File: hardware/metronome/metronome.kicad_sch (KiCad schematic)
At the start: 57 parts, among them J1 USB_C_Receptacle_USB2.0, J2 Conn_01x03_Pin, J3 Conn_01x04_Pin, J4 AudioJack3_Ground, SW1 RotaryEncoder_Switch, SW2 SW_SPST, SW3 SW_SPST, SW4 SW_SPST, SW5 SW_SPST, U1 ATtiny412, U2 ME6209A40PG, U3 FM8002, Y1 10MHz

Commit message: Version 02
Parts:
- removed C11: 0.33uF, Capacitor_SMD:C_0603_1608Metric_Pad1.08x0.95mm_HandSolder, symbol Device:C_Small
- removed H1: MountingHole, MountingHole:MountingHole_2.2mm_M2, symbol Mechanical:MountingHole
- removed J2: Conn_01x03_Pin, Connector_PinHeader_2.54mm:PinHeader_1x03_P2.54mm_Vertical, symbol Connector:Conn_01x03_Pin
- removed U3: FM8002, Package_SO:SOP-8-1EP_4.57x4.57mm_P1.27mm_EP4.57x4.45mm_ThermalVias, symbol EzerLonginus:FM8002A
- added C11, C13: 100uF, Capacitor_SMD:CP_Elec_6.3x5.4_Nichicon, symbol Device:C_Polarized_US
- added C14: 2.2uF, Capacitor_SMD:C_0805_2012Metric_Pad1.18x1.45mm_HandSolder, symbol Device:C_Small
- added C15: 0.1uF, Capacitor_SMD:C_0603_1608Metric_Pad1.08x0.95mm_HandSolder, symbol Device:C_Small
- added J2: Conn_01x04_Pin, ELonginus:1x4_2.54mm_pin_staggered, symbol Connector:Conn_01x04_Pin
- added R30, R31, R32: 3k9, Resistor_SMD:R_0603_1608Metric_Pad0.98x0.95mm_HandSolder, symbol Device:R_Small_US
- added U3: LM4808, Package_SO:SOIC-8_3.9x4.9mm_P1.27mm, symbol EzerLonginus:LM4808
- C10: value 1.0uF -> 1uF
- C12: value 1.0uF -> 2.2uF; footprint Capacitor_SMD:C_0603_1608Metric_Pad1.08x0.95mm_HandSolder -> Capacitor_SMD:C_0805_2012Metric_Pad1.18x1.45mm_HandSolder
- J4: footprint ELonginus:Jack_3.5mm_PJ320E_Horizontal -> ELonginus:6.35mm headphone jack PJ-611A
- R26: value 10k -> 100k
- R27: value 20k -> 100k
- R28: value 20k -> 3k9
- SW2, SW3: footprint Button_Switch_THT:SW_PUSH_6mm_H4.3mm -> ELonginus:SW_PUSH_6mm
- SW4, SW5: footprint Button_Switch_THT:SW_PUSH-12mm -> ELonginus:SW_PUSH_12mm
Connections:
- net +3.3V: now also R26.1, C15.1, J2.1 (Pin_1), U3.8 (VDD); no longer C12.1, R26.2
- net AUDIO_OUT: now also C12.1, C14.1
- net GND: now also R27.2, C15.2, J2.2 (Pin_2), U3.4 (GND); no longer C12.2
- net PA3: now also J2.4 (Pin_4)
- net UPDI: now also J2.3 (Pin_3)
- net at C10.1: now also R26.2, R27.1, U3.3 (INAP), U3.5 (INBP)
- net VOUT1: now reaches R28.2
- net VOUT1: now also C11.1, U3.1 (VOUT1); no longer R27.1
- net VO1: no longer names the net of R28.1
- net VO1: now also R30.2, U3.2 (INAN); no longer J4.R
- net VO2 renamed BC2
- net BC2: now also C13.2
- new net: C12.2, R30.1
- new net: R31.1, R32.2, U3.6 (INBN)
- new net: C14.2, R32.1
- new net BC1: C11.2, J4.R
- new net VOUT2: C13.1, R31.2, U3.7 (VOUT2)
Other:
- note added: "PA3 BREAKOUT"
- title: (none) -> Metronome
- moved on the sheet: C1, C2, C3, C4, C5, C6, H2, J3, J4, R1, R10, R11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

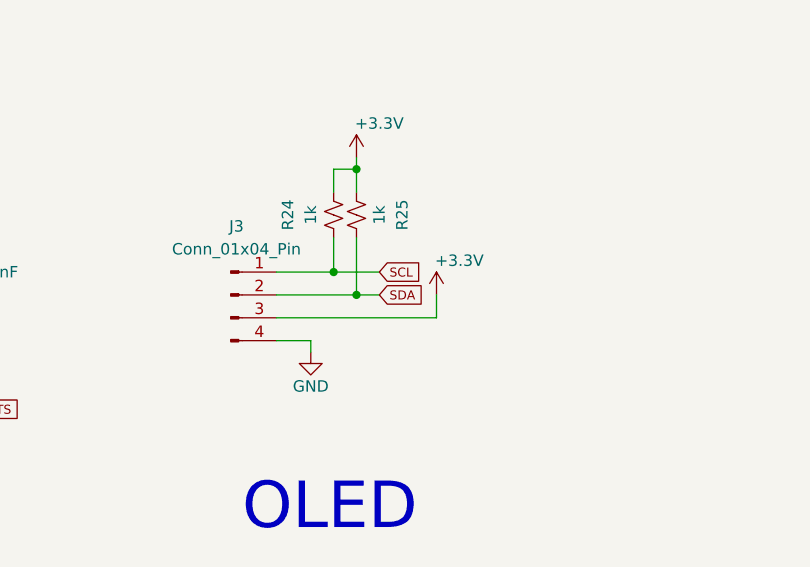
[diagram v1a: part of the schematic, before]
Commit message: pin swap
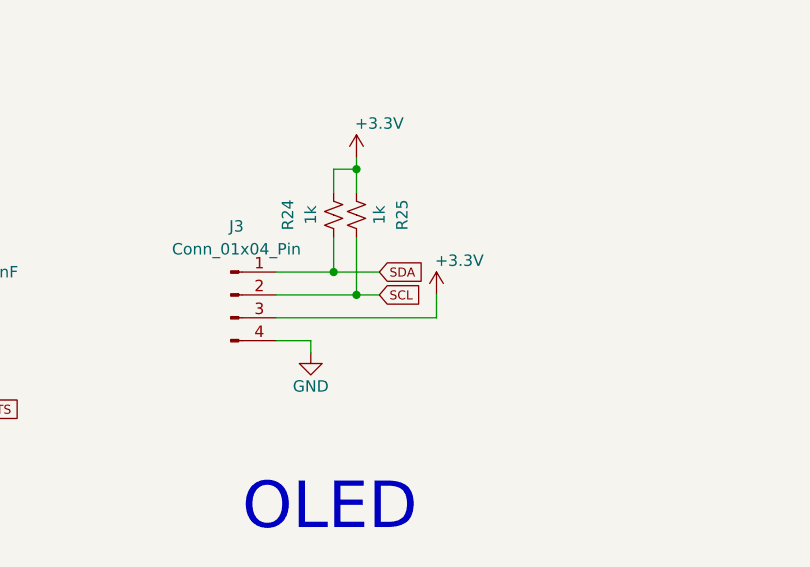
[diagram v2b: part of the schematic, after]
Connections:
- net SCL: now also J3.2 (Pin_2), R25.1; no longer J3.1 (Pin_1), R24.1
- net SDA: now also J3.1 (Pin_1), R24.1; no longer J3.2 (Pin_2), R25.1
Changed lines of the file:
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@@
     )
   )
-  (global_label "SDA" (shape input) (at 154.94 165.1 0) (fields_autoplaced)
+  (global_label "SDA" (shape input) (at 154.94 162.56 0) (fields_autoplaced)
     (effects (font (size 1 1)) (justify left))
-    (property "Intersheetrefs" "${INTERSHEET_REFS}" (at 160.0998 165.1 0)
+    (property "Intersheetrefs" "${INTERSHEET_REFS}" (at 160.0998 162.56 0)
       (effects (font (size 1.27 1.27)) (justify left) hide)
     )
@@
     )
   )
-  (global_label "SCL" (shape input) (at 154.94 162.56 0) (fields_autoplaced)
+  (global_label "SCL" (shape input) (at 154.94 165.1 0) (fields_autoplaced)
     (effects (font (size 1 1)) (justify left))
-    (property "Intersheetrefs" "${INTERSHEET_REFS}" (at 160.0522 162.56 0)
+    (property "Intersheetrefs" "${INTERSHEET_REFS}" (at 160.0522 165.1 0)
       (effects (font (size 1.27 1.27)) (justify left) hide)
     )
